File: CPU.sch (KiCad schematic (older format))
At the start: 23 parts

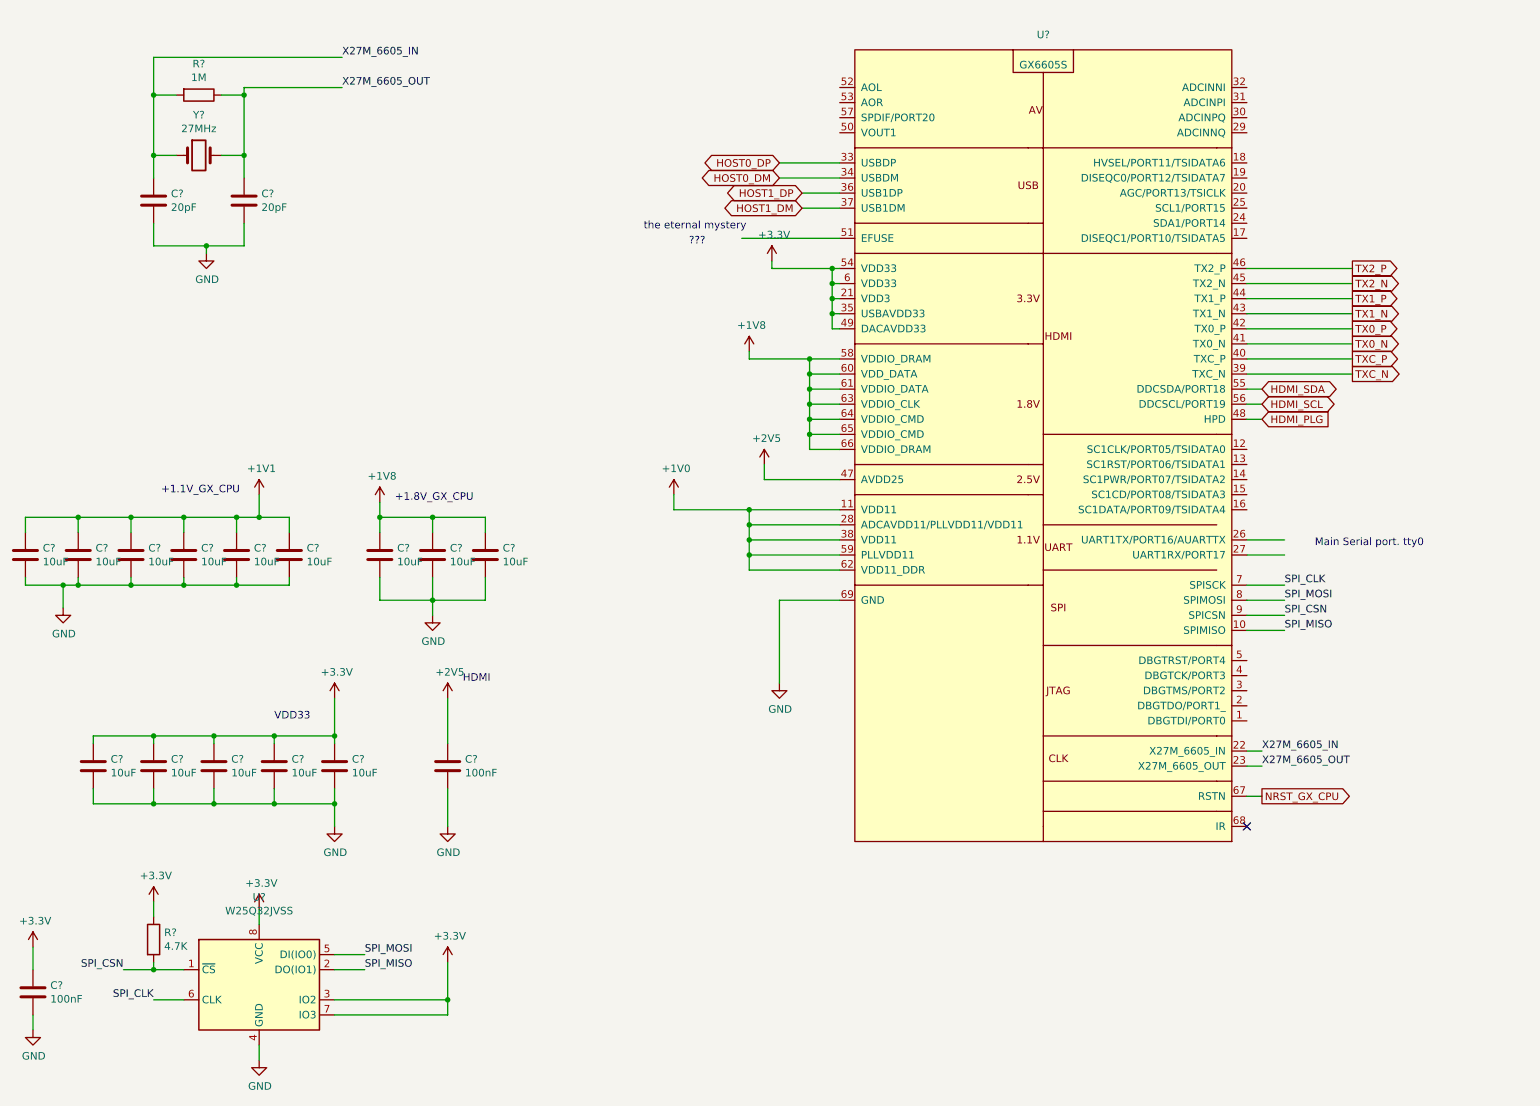
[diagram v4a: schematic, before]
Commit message: broke, out all GPIO and finsihed wiring HDMI
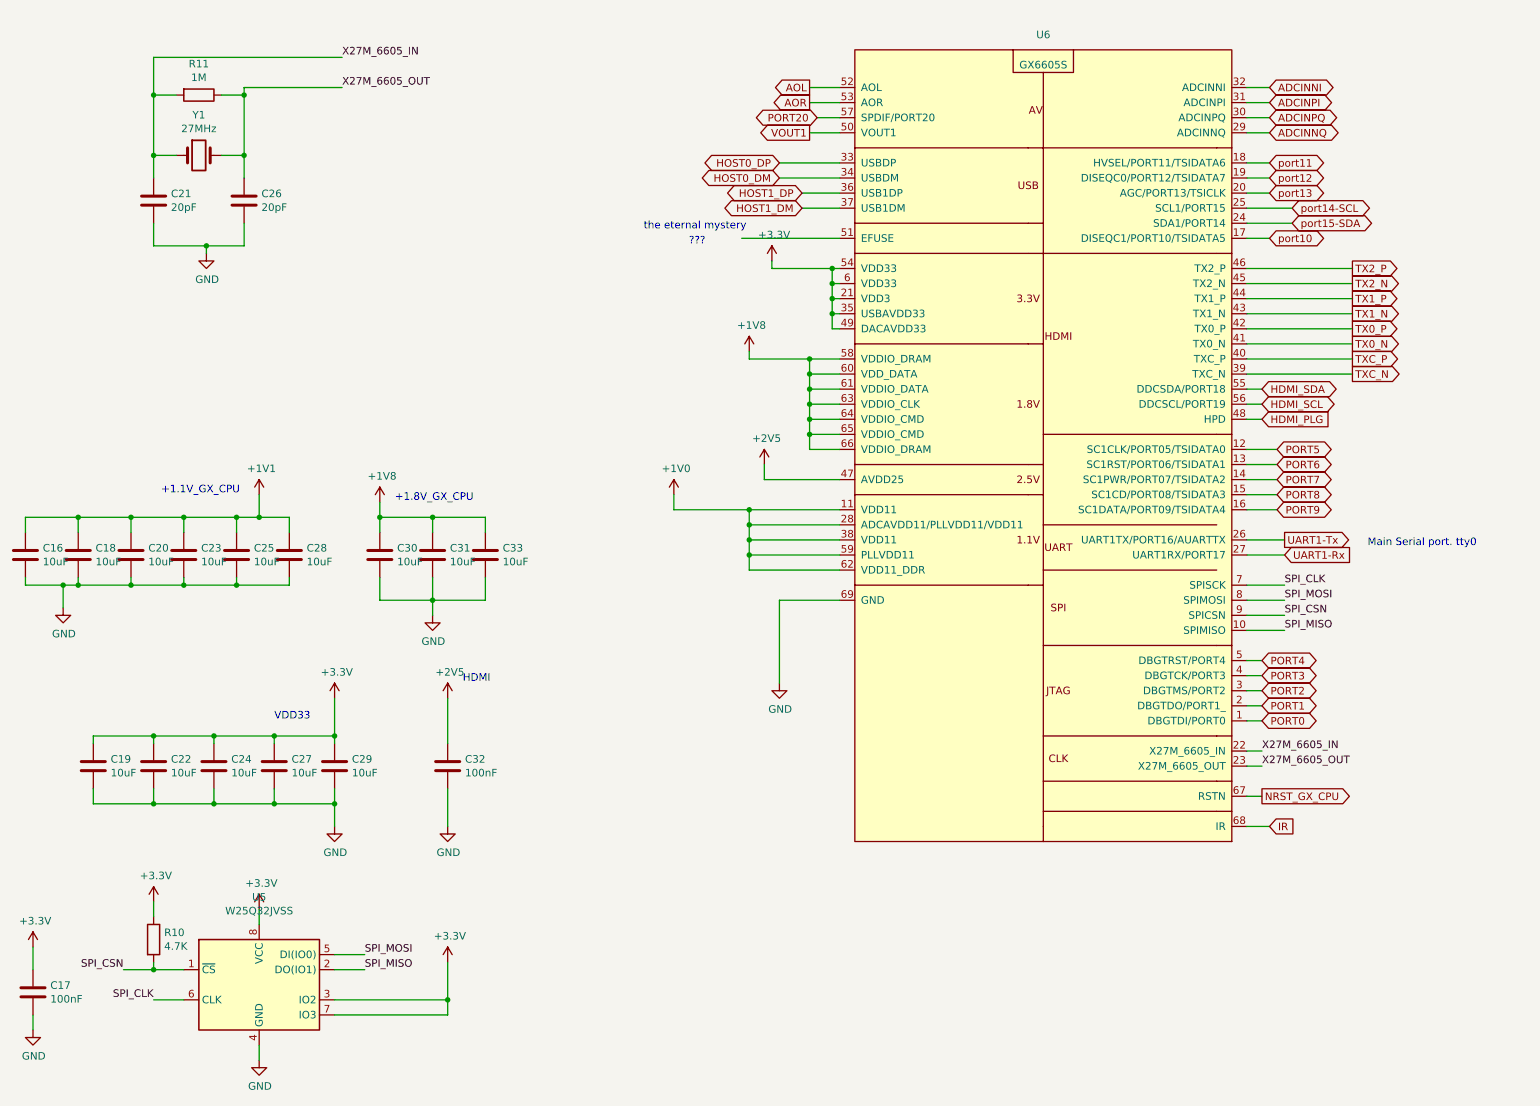
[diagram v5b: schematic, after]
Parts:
- gave numbers to parts that had none: 23
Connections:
- net PORT0: now reaches U6.1 (DBGTDI/PORT0)
- net PORT5: now reaches U6.12 (SC1CLK/PORT05/TSIDATA0)
- net PORT6: now reaches U6.13 (SC1RST/PORT06/TSIDATA1)
- net PORT7: now reaches U6.14 (SC1PWR/PORT07/TSIDATA2)
- net PORT8: now reaches U6.15 (SC1CD/PORT08/TSIDATA3)
- net PORT9: now reaches U6.16 (SC1DATA/PORT09/TSIDATA4)
- net port10: now reaches U6.17 (DISEQC1/PORT10/TSIDATA5)
- net port11: now reaches U6.18 (HVSEL/PORT11/TSIDATA6)
- net port12: now reaches U6.19 (DISEQC0/PORT12/TSIDATA7)
- net PORT1: now reaches U6.2 (DBGTDO/PORT1_)
- net port13: now reaches U6.20 (AGC/PORT13/TSICLK)
- net port15-SDA: now reaches U6.24 (SDA1/PORT14)
- net port14-SCL: now reaches U6.25 (SCL1/PORT15)
- net UART1-Tx: now reaches U6.26 (UART1TX/PORT16/AUARTTX)
- net UART1-Rx: now reaches U6.27 (UART1RX/PORT17)
- net ADCINNQ: now reaches U6.29 (ADCINNQ)
- net PORT2: now reaches U6.3 (DBGTMS/PORT2)
- net ADCINPQ: now reaches U6.30 (ADCINPQ)
- net ADCINPI: now reaches U6.31 (ADCINPI)
- net ADCINNI: now reaches U6.32 (ADCINNI)
- net PORT3: now reaches U6.4 (DBGTCK/PORT3)
- net PORT4: now reaches U6.5 (DBGTRST/PORT4)
- net VOUT1: now reaches U6.50 (VOUT1)
- net AOL: now reaches U6.52 (AOL)
- net AOR: now reaches U6.53 (AOR)
- net PORT20: now reaches U6.57 (SPDIF/PORT20)
- net IR: now reaches U6.68 (IR)
- no-connect marks 1 -> 0

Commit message: finished scimatic for now, and started populating PCB. *chugs rrum*
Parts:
- C16, C17, C18, C19, C20, C21, C22, C23, C24, C25, C26, C27, C28, C29, C30, C31, C32, C33: footprint (none) -> Capacitor_SMD:C_0402_1005Metric
- R10, R11: footprint (none) -> Resistor_SMD:R_0402_1005Metric
- U6: footprint (none) -> Package_DFN_QFN:QFN-68-1EP_8x8mm_P0.4mm_EP5.2x5.2mm_ThermalVias
- Y1: footprint (none) -> Crystal:Crystal_SMD_7050-2Pin_7.0x5.0mm
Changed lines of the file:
@@
 $Descr A4 11693 8268
 encoding utf-8
-Sheet 3 4
+Sheet 3 5
 Title ""
 Date ""
@@
 F 0 "C26" H 2265 1946 50  0000 L CNN
 F 1 "20pF" H 2265 1855 50  0000 L CNN
-F 2 "" H 2188 1750 50  0001 C CNN
+F 2 "Capacitor_SMD:C_0402_1005Metric" H 2188 1750 50  0001 C CNN
 F 3 "~" H 2150 1900 50  0001 C CNN
 	1    2150 1900
@@
 F 0 "C21" H 1665 1946 50  0000 L CNN
 F 1 "20pF" H 1665 1855 50  0000 L CNN
-F 2 "" H 1588 1750 50  0001 C CNN
+F 2 "Capacitor_SMD:C_0402_1005Metric" H 1588 1750 50  0001 C CNN
 F 3 "~" H 1550 1900 50  0001 C CNN
 	1    1550 1900
@@
 F 0 "Y1" H 1850 1868 50  0000 C CNN
 F 1 "27MHz" H 1850 1777 50  0000 C CNN
-F 2 "" H 1850 1600 50  0001 C CNN
+F 2 "Crystal:Crystal_SMD_7050-2Pin_7.0x5.0mm" H 1850 1600 50  0001 C CNN
 F 3 "~" H 1850 1600 50  0001 C CNN
 	1    1850 1600
@@
 F 0 "U6" H 7450 1400 50  0000 C CNN
 F 1 "GX6605S" H 7450 1200 50  0000 C CNN
-F 2 "" H 7350 1250 50  0001 C CNN
+F 2 "Package_DFN_QFN:QFN-68-1EP_8x8mm_P0.4mm_EP5.2x5.2mm_ThermalVias" H 7350 1250 50  0001 C CNN
 F 3 "" H 7350 1250 50  0001 C CNN
 	1    7450 1100
@@
 F 0 "R11" V 1643 1200 50  0000 C CNN
 F 1 "1M" V 1734 1200 50  0000 C CNN
-F 2 "" V 1780 1200 50  0001 C CNN
+F 2 "Resistor_SMD:R_0402_1005Metric" V 1780 1200 50  0001 C CNN
 F 3 "~" H 1850 1200 50  0001 C CNN
 	1    1850 1200
@@
 F 0 "C19" H 1265 5696 50  0000 L CNN
 F 1 "10uF" H 1265 5605 50  0000 L CNN
-F 2 "" H 1188 5500 50  0001 C CNN
+F 2 "Capacitor_SMD:C_0402_1005Metric" H 1188 5500 50  0001 C CNN
 F 3 "~" H 1150 5650 50  0001 C CNN
 	1    1150 5650
@@
 F 0 "C22" H 1665 5696 50  0000 L CNN
 F 1 "10uF" H 1665 5605 50  0000 L CNN
-F 2 "" H 1588 5500 50  0001 C CNN
+F 2 "Capacitor_SMD:C_0402_1005Metric" H 1588 5500 50  0001 C CNN
 F 3 "~" H 1550 5650 50  0001 C CNN
 	1    1550 5650
@@
 F 0 "C24" H 2065 5696 50  0000 L CNN
 F 1 "10uF" H 2065 5605 50  0000 L CNN
-F 2 "" H 1988 5500 50  0001 C CNN
+F 2 "Capacitor_SMD:C_0402_1005Metric" H 1988 5500 50  0001 C CNN
 F 3 "~" H 1950 5650 50  0001 C CNN
 	1    1950 5650
@@
 F 0 "C27" H 2465 5696 50  0000 L CNN
 F 1 "10uF" H 2465 5605 50  0000 L CNN
-F 2 "" H 2388 5500 50  0001 C CNN
+F 2 "Capacitor_SMD:C_0402_1005Metric" H 2388 5500 50  0001 C CNN
 F 3 "~" H 2350 5650 50  0001 C CNN
 	1    2350 5650
@@
 F 0 "C29" H 2865 5696 50  0000 L CNN
 F 1 "10uF" H 2865 5605 50  0000 L CNN
-F 2 "" H 2788 5500 50  0001 C CNN
+F 2 "Capacitor_SMD:C_0402_1005Metric" H 2788 5500 50  0001 C CNN
 F 3 "~" H 2750 5650 50  0001 C CNN
 	1    2750 5650
@@
 F 0 "C32" H 3615 5696 50  0000 L CNN
 F 1 "100nF" H 3615 5605 50  0000 L CNN
-F 2 "" H 3538 5500 50  0001 C CNN
+F 2 "Capacitor_SMD:C_0402_1005Metric" H 3538 5500 50  0001 C CNN
 F 3 "~" H 3500 5650 50  0001 C CNN
 	1    3500 5650
@@
 F 0 "C16" H 815 4296 50  0000 L CNN
 F 1 "10uF" H 815 4205 50  0000 L CNN
-F 2 "" H 738 4100 50  0001 C CNN
+F 2 "Capacitor_SMD:C_0402_1005Metric" H 738 4100 50  0001 C CNN
 F 3 "~" H 700 4250 50  0001 C CNN
 	1    700  4250
@@
 F 0 "C18" H 1165 4296 50  0000 L CNN
 F 1 "10uF" H 1165 4205 50  0000 L CNN
-F 2 "" H 1088 4100 50  0001 C CNN
+F 2 "Capacitor_SMD:C_0402_1005Metric" H 1088 4100 50  0001 C CNN
 F 3 "~" H 1050 4250 50  0001 C CNN
 	1    1050 4250
@@
 F 0 "C20" H 1515 4296 50  0000 L CNN
 F 1 "10uF" H 1515 4205 50  0000 L CNN
-F 2 "" H 1438 4100 50  0001 C CNN
+F 2 "Capacitor_SMD:C_0402_1005Metric" H 1438 4100 50  0001 C CNN
 F 3 "~" H 1400 4250 50  0001 C CNN
 	1    1400 4250
@@
 F 0 "C23" H 1865 4296 50  0000 L CNN
 F 1 "10uF" H 1865 4205 50  0000 L CNN
-F 2 "" H 1788 4100 50  0001 C CNN
+F 2 "Capacitor_SMD:C_0402_1005Metric" H 1788 4100 50  0001 C CNN
 F 3 "~" H 1750 4250 50  0001 C CNN
 	1    1750 4250
@@
 F 0 "C25" H 2215 4296 50  0000 L CNN
 F 1 "10uF" H 2215 4205 50  0000 L CNN
-F 2 "" H 2138 4100 50  0001 C CNN
+F 2 "Capacitor_SMD:C_0402_1005Metric" H 2138 4100 50  0001 C CNN
 F 3 "~" H 2100 4250 50  0001 C CNN
 	1    2100 4250
@@
 F 0 "C28" H 2565 4296 50  0000 L CNN
 F 1 "10uF" H 2565 4205 50  0000 L CNN
-F 2 "" H 2488 4100 50  0001 C CNN
+F 2 "Capacitor_SMD:C_0402_1005Metric" H 2488 4100 50  0001 C CNN
 F 3 "~" H 2450 4250 50  0001 C CNN
 	1    2450 4250
@@
 F 0 "C30" H 3165 4296 50  0000 L CNN
 F 1 "10uF" H 3165 4205 50  0000 L CNN
-F 2 "" H 3088 4100 50  0001 C CNN
+F 2 "Capacitor_SMD:C_0402_1005Metric" H 3088 4100 50  0001 C CNN
 F 3 "~" H 3050 4250 50  0001 C CNN
 	1    3050 4250
@@
 F 0 "C31" H 3515 4296 50  0000 L CNN
 F 1 "10uF" H 3515 4205 50  0000 L CNN
-F 2 "" H 3438 4100 50  0001 C CNN
+F 2 "Capacitor_SMD:C_0402_1005Metric" H 3438 4100 50  0001 C CNN
 F 3 "~" H 3400 4250 50  0001 C CNN
 	1    3400 4250
@@
 F 0 "C33" H 3865 4296 50  0000 L CNN
 F 1 "10uF" H 3865 4205 50  0000 L CNN
-F 2 "" H 3788 4100 50  0001 C CNN
+F 2 "Capacitor_SMD:C_0402_1005Metric" H 3788 4100 50  0001 C CNN
 F 3 "~" H 3750 4250 50  0001 C CNN
 	1    3750 4250
@@
 F 0 "C17" H 865 7196 50  0000 L CNN
 F 1 "100nF" H 865 7105 50  0000 L CNN
-F 2 "" H 788 7000 50  0001 C CNN
+F 2 "Capacitor_SMD:C_0402_1005Metric" H 788 7000 50  0001 C CNN
 F 3 "~" H 750 7150 50  0001 C CNN
 	1    750  7150
@@
 F 0 "R10" H 1620 6846 50  0000 L CNN
 F 1 "4.7K" H 1620 6755 50  0000 L CNN
-F 2 "" V 1480 6800 50  0001 C CNN
+F 2 "Resistor_SMD:R_0402_1005Metric" V 1480 6800 50  0001 C CNN
 F 3 "~" H 1550 6800 50  0001 C CNN
 	1    1550 6800

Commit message: started layout of the PCB, allso moved onto craken rum, from captin morgan. please for the love of god check the footprints are right. @MAX
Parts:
- Y1: footprint Crystal:Crystal_SMD_7050-2Pin_7.0x5.0mm -> Crystal:Crystal_SMD_2012-2Pin_2.0x1.2mm_HandSoldering
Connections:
- net +1V0 is gone; now on net +1V1: U6.11 (VDD11), U6.28 (ADCAVDD11/PLLVDD11/VDD11), U6.38 (VDD11), U6.59 (PLLVDD11), U6.62 (VDD11_DDR)
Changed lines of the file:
@@
 F 0 "Y1" H 1850 1868 50  0000 C CNN
 F 1 "27MHz" H 1850 1777 50  0000 C CNN
-F 2 "Crystal:Crystal_SMD_7050-2Pin_7.0x5.0mm" H 1850 1600 50  0001 C CNN
+F 2 "Crystal:Crystal_SMD_2012-2Pin_2.0x1.2mm_HandSoldering" H 1850 1600 50  0001 C CNN
 F 3 "~" H 1850 1600 50  0001 C CNN
 	1    1850 1600
@@
 	5000 3950 5000 3850
 Connection ~ 5500 3950
-$Comp
-L power:+1V0 #PWR0137
-U 1 1 5F51B756
-P 5000 3850
-F 0 "#PWR0137" H 5000 3700 50  0001 C CNN
-F 1 "+1V0" H 5015 4023 50  0000 C CNN
-F 2 "" H 5000 3850 50  0001 C CNN
-F 3 "" H 5000 3850 50  0001 C CNN
-	1    5000 3850
-	1    0    0    -1
-$EndComp
 $Comp
 L power:+1V8 #PWR0138
@@
 Wire Wire Line
 	8900 5350 8800 5350
+$Comp
+L power:+1V1 #PWR0137
+U 1 1 5F69D32E
+P 5000 3850
+F 0 "#PWR0137" H 5000 3700 50  0001 C CNN
+F 1 "+1V1" H 5015 4023 50  0000 C CNN
+F 2 "" H 5000 3850 50  0001 C CNN
+F 3 "" H 5000 3850 50  0001 C CNN
+	1    5000 3850
+	1    0    0    -1
+$EndComp
 $EndSCHEMATC

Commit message: did some routing and fixed some pinouts on components
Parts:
- added TP1: TestPoint, TestPoint:TestPoint_Pad_1.0x1.0mm, symbol Connector:TestPoint
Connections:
- net at U6.51 (EFUSE): now also TP1.1
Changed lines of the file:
@@
 Wire Wire Line
 	6100 2150 5450 2150
-Text Notes 4800 2100 0    50   ~ 0
+Text Notes 4450 2100 0    50   ~ 0
 the eternal mystery
 Text Notes 5100 2200 0    50   ~ 0
@@
 P 5650 2300
 F 0 "#PWR0134" H 5650 2150 50  0001 C CNN
-F 1 "+3.3V" H 5665 2473 50  0000 C CNN
+F 1 "+3.3V" H 5500 2300 50  0000 C CNN
 F 2 "" H 5650 2300 50  0001 C CNN
 F 3 "" H 5650 2300 50  0001 C CNN
@@
 	1    0    0    -1
 $EndComp
+$Comp
+L Connector:TestPoint TP1
+U 1 1 604BDA66
+P 5450 2150
+F 0 "TP1" V 5500 1950 50  0000 C CNN
+F 1 "TestPoint" V 5550 2200 50  0000 C CNN
+F 2 "TestPoint:TestPoint_Pad_1.0x1.0mm" H 5650 2150 50  0001 C CNN
+F 3 "~" H 5650 2150 50  0001 C CNN
+	1    5450 2150
+	0    -1   -1   0
+$EndComp
 $EndSCHEMATC
